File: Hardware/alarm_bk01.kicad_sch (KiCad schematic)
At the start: 18 parts, among them Q1 2N3904, SW1 START, SW2 Sensor, SW3 SW_SPDT, U1 ATtiny85V-10P

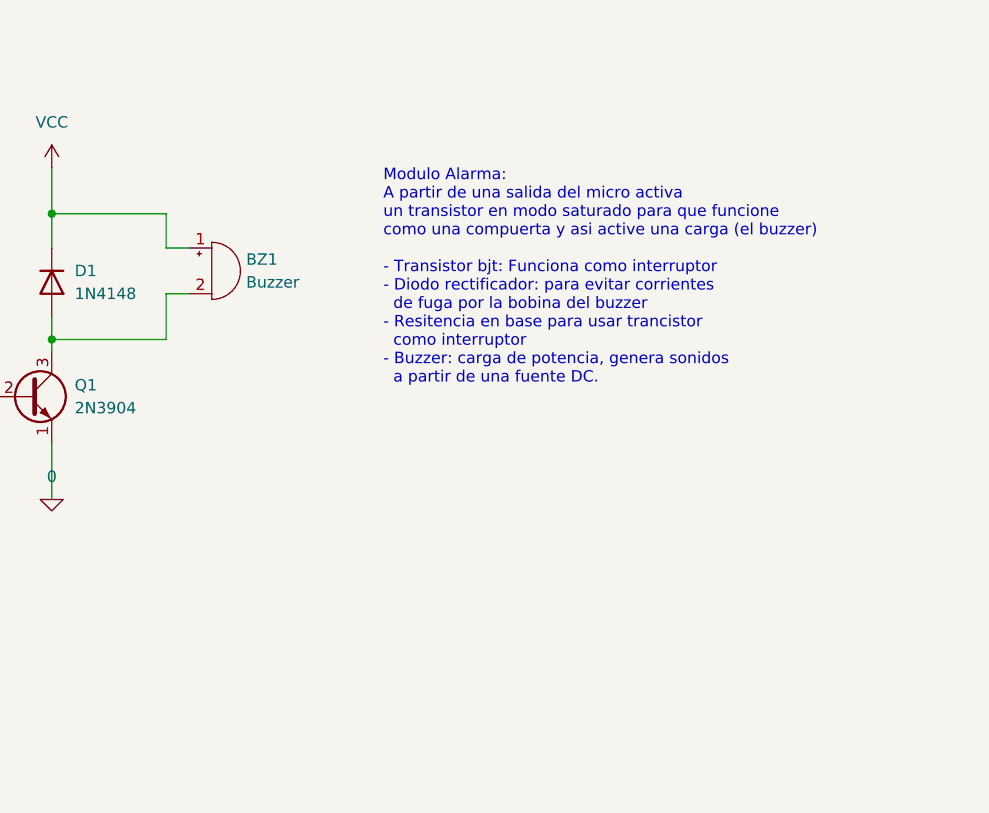
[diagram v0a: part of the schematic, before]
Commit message: reorganice components
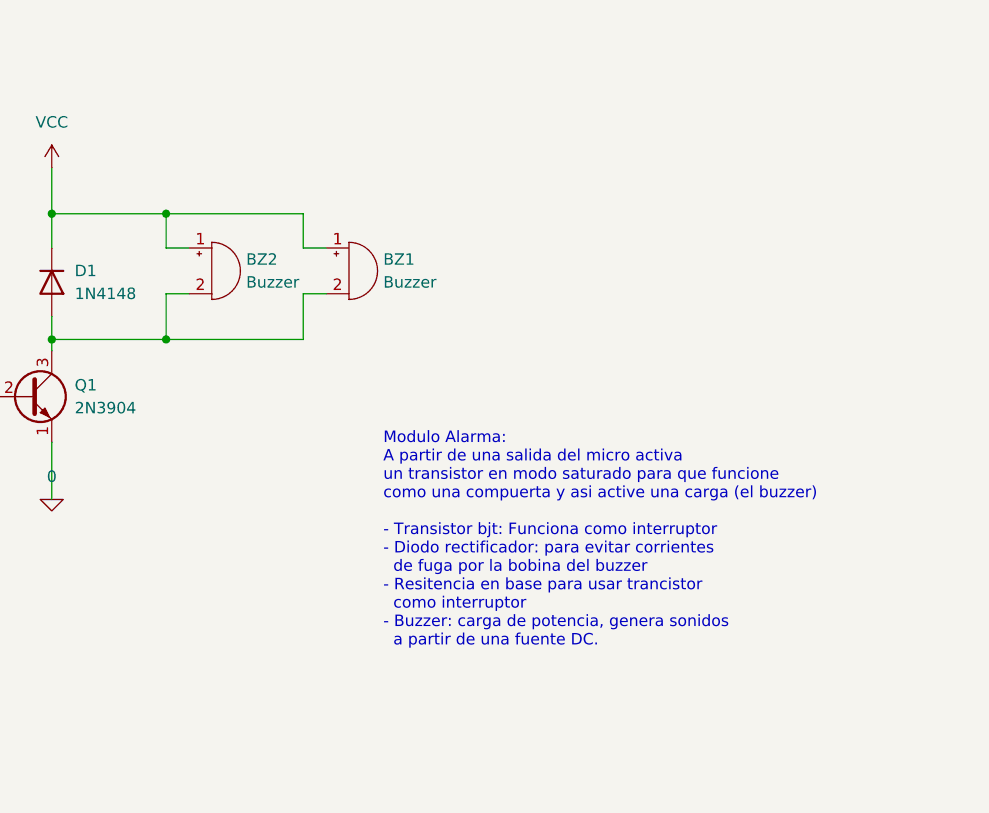
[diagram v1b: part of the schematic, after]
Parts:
- added BZ2: Buzzer, Connector_JST:JST_EH_B2B-EH-A_1x02_P2.50mm_Vertical, symbol Device:Buzzer
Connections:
- net VCC: now also BZ2.1 (-)
- net at BZ1.2 (+), D1.2 (A), Q1.3 (C): now also BZ2.2 (+)
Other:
- moved on the sheet: BZ1
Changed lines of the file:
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@@
   (junction (at 73.66 33.02) (diameter 0) (color 0 0 0 0)
   )
+  (junction (at 196.85 93.98) (diameter 0) (color 0 0 0 0)
+  )
+  (junction (at 196.85 107.95) (diameter 0) (color 0 0 0 0)
+  )
   (wire (pts (xy 69.85 181.61) (xy 69.85 186.69))
     (stroke (width 0) (type default) (color 0 0 0 0))
@@
     (stroke (width 0) (type default) (color 0 0 0 0))
   )
+  (wire (pts (xy 196.85 102.87) (xy 196.85 107.95))
+    (stroke (width 0) (type default) (color 0 0 0 0))
+  )
   (wire (pts (xy 40.64 119.38) (xy 40.64 125.73))
     (stroke (width 0) (type default) (color 0 0 0 0))
@@
     (stroke (width 0) (type default) (color 0 0 0 0))
   )
+  (wire (pts (xy 199.39 97.79) (xy 196.85 97.79))
+    (stroke (width 0) (type default) (color 0 0 0 0))
+  )
   (wire (pts (xy 140.97 24.13) (xy 140.97 30.48))
     (stroke (width 0) (type default) (color 0 0 0 0))
   )
-  (wire (pts (xy 196.85 102.87) (xy 196.85 107.95))
-    (stroke (width 0) (type default) (color 0 0 0 0))
-  )
   (wire (pts (xy 73.66 29.21) (xy 73.66 33.02))
     (stroke (width 0) (type default) (color 0 0 0 0))
@@
     (stroke (width 0) (type default) (color 0 0 0 0))
   )
-  (wire (pts (xy 196.85 102.87) (xy 199.39 102.87))
-    (stroke (width 0) (type default) (color 0 0 0 0))
-  )
   (wire (pts (xy 30.48 48.26) (xy 30.48 53.34))
     (stroke (width 0) (type default) (color 0 0 0 0))
   )
+  (wire (pts (xy 184.15 93.98) (xy 196.85 93.98))
+    (stroke (width 0) (type default) (color 0 0 0 0))
+  )
+  (wire (pts (xy 140.97 49.53) (xy 140.97 55.88))
+    (stroke (width 0) (type default) (color 0 0 0 0))
+  )
+  (wire (pts (xy 212.09 102.87) (xy 214.63 102.87))
+    (stroke (width 0) (type default) (color 0 0 0 0))
+  )
+  (wire (pts (xy 184.15 88.9) (xy 184.15 93.98))
+    (stroke (width 0) (type default) (color 0 0 0 0))
+  )
+  (wire (pts (xy 45.72 33.02) (xy 46.99 33.02))
+    (stroke (width 0) (type default) (color 0 0 0 0))
+  )
+  (wire (pts (xy 171.45 114.3) (xy 176.53 114.3))
+    (stroke (width 0) (type default) (color 0 0 0 0))
+  )
+  (wire (pts (xy 140.97 38.1) (xy 140.97 41.91))
+    (stroke (width 0) (type default) (color 0 0 0 0))
+  )
+  (wire (pts (xy 184.15 107.95) (xy 184.15 109.22))
+    (stroke (width 0) (type default) (color 0 0 0 0))
+  )
+  (wire (pts (xy 196.85 107.95) (xy 212.09 107.95))
+    (stroke (width 0) (type default) (color 0 0 0 0))
+  )
+  (wire (pts (xy 161.29 114.3) (xy 163.83 114.3))
+    (stroke (width 0) (type default) (color 0 0 0 0))
+  )
+  (wire (pts (xy 44.45 109.22) (xy 40.64 109.22))
+    (stroke (width 0) (type default) (color 0 0 0 0))
+  )
+  (wire (pts (xy 73.66 33.02) (xy 73.66 38.1))
+    (stroke (width 0) (type default) (color 0 0 0 0))
+  )
+  (wire (pts (xy 46.99 80.01) (xy 46.99 93.98))
+    (stroke (width 0) (type default) (color 0 0 0 0))
+  )
+  (wire (pts (xy 40.64 93.98) (xy 46.99 93.98))
+    (stroke (width 0) (type default) (color 0 0 0 0))
+  )
+  (wire (pts (xy 73.66 45.72) (xy 73.66 53.34))
+    (stroke (width 0) (type default) (color 0 0 0 0))
+  )
+  (wire (pts (xy 30.48 33.02) (xy 45.72 33.02))
+    (stroke (width 0) (type default) (color 0 0 0 0))
+  )
   (wire (pts (xy 196.85 97.79) (xy 196.85 93.98))
     (stroke (width 0) (type default) (color 0 0 0 0))
   )
-  (wire (pts (xy 184.15 93.98) (xy 196.85 93.98))
-    (stroke (width 0) (type default) (color 0 0 0 0))
-  )
-  (wire (pts (xy 140.97 49.53) (xy 140.97 55.88))
-    (stroke (width 0) (type default) (color 0 0 0 0))
-  )
-  (wire (pts (xy 184.15 88.9) (xy 184.15 93.98))
-    (stroke (width 0) (type default) (color 0 0 0 0))
-  )
-  (wire (pts (xy 45.72 33.02) (xy 46.99 33.02))
-    (stroke (width 0) (type default) (color 0 0 0 0))
-  )
-  (wire (pts (xy 171.45 114.3) (xy 176.53 114.3))
-    (stroke (width 0) (type default) (color 0 0 0 0))
-  )
-  (wire (pts (xy 140.97 38.1) (xy 140.97 41.91))
-    (stroke (width 0) (type default) (color 0 0 0 0))
-  )
-  (wire (pts (xy 184.15 107.95) (xy 184.15 109.22))
-    (stroke (width 0) (type default) (color 0 0 0 0))
-  )
-  (wire (pts (xy 161.29 114.3) (xy 163.83 114.3))
-    (stroke (width 0) (type default) (color 0 0 0 0))
-  )
-  (wire (pts (xy 44.45 109.22) (xy 40.64 109.22))
-    (stroke (width 0) (type default) (color 0 0 0 0))
-  )
-  (wire (pts (xy 73.66 33.02) (xy 73.66 38.1))
-    (stroke (width 0) (type default) (color 0 0 0 0))
-  )
-  (wire (pts (xy 46.99 80.01) (xy 46.99 93.98))
-    (stroke (width 0) (type default) (color 0 0 0 0))
-  )
-  (wire (pts (xy 40.64 93.98) (xy 46.99 93.98))
-    (stroke (width 0) (type default) (color 0 0 0 0))
-  )
-  (wire (pts (xy 73.66 45.72) (xy 73.66 53.34))
-    (stroke (width 0) (type default) (color 0 0 0 0))
-  )
-  (wire (pts (xy 30.48 33.02) (xy 45.72 33.02))
+  (wire (pts (xy 199.39 102.87) (xy 196.85 102.87))
     (stroke (width 0) (type default) (color 0 0 0 0))
   )
@@
     (stroke (width 0) (type default) (color 0 0 0 0))
   )
+  (wire (pts (xy 212.09 93.98) (xy 212.09 97.79))
+    (stroke (width 0) (type default) (color 0 0 0 0))
+  )
   (wire (pts (xy 57.15 33.02) (xy 62.23 33.02))
     (stroke (width 0) (type default) (color 0 0 0 0))
@@
     (stroke (width 0) (type default) (color 0 0 0 0))
   )
+  (wire (pts (xy 212.09 97.79) (xy 214.63 97.79))
+    (stroke (width 0) (type default) (color 0 0 0 0))
+  )
   (wire (pts (xy 44.45 105.41) (xy 44.45 109.22))
     (stroke (width 0) (type default) (color 0 0 0 0))
@@
     (stroke (width 0) (type default) (color 0 0 0 0))
   )
-  (wire (pts (xy 199.39 97.79) (xy 196.85 97.79))
+  (wire (pts (xy 196.85 93.98) (xy 212.09 93.98))
     (stroke (width 0) (type default) (color 0 0 0 0))
   )
@@
   )
   (wire (pts (xy 45.72 45.72) (xy 45.72 53.34))
+    (stroke (width 0) (type default) (color 0 0 0 0))
+  )
+  (wire (pts (xy 212.09 107.95) (xy 212.09 102.87))
     (stroke (width 0) (type default) (color 0 0 0 0))
   )
@@
   )
   (text "Modulo Alarma:\nA partir de una salida del micro activa \nun transistor en modo saturado para que funcione\ncomo una compuerta y asi active una carga (el buzzer)\n\n- Transistor bjt: Funciona como interruptor\n- Diodo rectificador: para evitar corrientes \n  de fuga por la bobina del buzzer\n- Resitencia en base para usar trancistor \n  como interruptor\n- Buzzer: carga de potencia, genera sonidos\n  a partir de una fuente DC."
-    (at 220.98 113.03 0)
+    (at 220.98 142.24 0)
     (effects (font (size 1.27 1.27)) (justify left bottom))
   )
@@
     (pin "2")
   )
-  (symbol (lib_id "Device:Buzzer") (at 201.93 100.33 0) (unit 1)
-    (in_bom yes) (on_board yes) (fields_autoplaced)
-    (property "Reference" "BZ1" (id 0) (at 205.74 99.0599 0)
-      (effects (font (size 1.27 1.27)) (justify left))
-    )
-    (property "Value" "Buzzer" (id 1) (at 205.74 101.5999 0)
-      (effects (font (size 1.27 1.27)) (justify left))
-    )
-    (property "Footprint" "Connector_JST:JST_EH_B2B-EH-A_1x02_P2.50mm_Vertical" (id 2) (at 201.295 97.79 90)
-      (effects (font (size 1.27 1.27)) hide)
-    )
-    (property "Datasheet" "~" (id 3) (at 201.295 97.79 90)
+  (symbol (lib_id "Device:Buzzer") (at 217.17 100.33 0) (unit 1)
+    (in_bom yes) (on_board yes) (fields_autoplaced)
+    (property "Reference" "BZ1" (id 0) (at 220.98 99.0599 0)
+      (effects (font (size 1.27 1.27)) (justify left))
+    )
+    (property "Value" "Buzzer" (id 1) (at 220.98 101.5999 0)
+      (effects (font (size 1.27 1.27)) (justify left))
+    )
+    (property "Footprint" "Connector_JST:JST_EH_B2B-EH-A_1x02_P2.50mm_Vertical" (id 2) (at 216.535 97.79 90)
+      (effects (font (size 1.27 1.27)) hide)
+    )
+    (property "Datasheet" "~" (id 3) (at 216.535 97.79 90)
       (effects (font (size 1.27 1.27)) hide)
     )
@@
     (pin "2")
     (pin "3")
+  )
+  (symbol (lib_id "Device:Buzzer") (at 201.93 100.33 0) (unit 1)
+    (in_bom yes) (on_board yes) (fields_autoplaced)
+    (property "Reference" "BZ2" (id 0) (at 205.74 99.0599 0)
+      (effects (font (size 1.27 1.27)) (justify left))
+    )
+    (property "Value" "Buzzer" (id 1) (at 205.74 101.5999 0)
+      (effects (font (size 1.27 1.27)) (justify left))
+    )
+    (property "Footprint" "Connector_JST:JST_EH_B2B-EH-A_1x02_P2.50mm_Vertical" (id 2) (at 201.295 97.79 90)
+      (effects (font (size 1.27 1.27)) hide)
+    )
+    (property "Datasheet" "~" (id 3) (at 201.295 97.79 90)
+      (effects (font (size 1.27 1.27)) hide)
+    )
+    (pin "1")
+    (pin "2")
   )
   (symbol (lib_id "MCU_Microchip_ATtiny:ATtiny85V-10P") (at 69.85 166.37 0) (mirror y) (unit 1)
@@
       (reference "BZ1") (unit 1) (value "Buzzer") (footprint "Connector_JST:JST_EH_B2B-EH-A_1x02_P2.50mm_Vertical")
     )
+    (path "/ba9d4216-b458-4eff-8d50-21ed5423f5fa"
+      (reference "BZ2") (unit 1) (value "Buzzer") (footprint "Connector_JST:JST_EH_B2B-EH-A_1x02_P2.50mm_Vertical")
+    )
     (path "/f9d78065-9a5e-4d58-b424-72b0930f1c67"

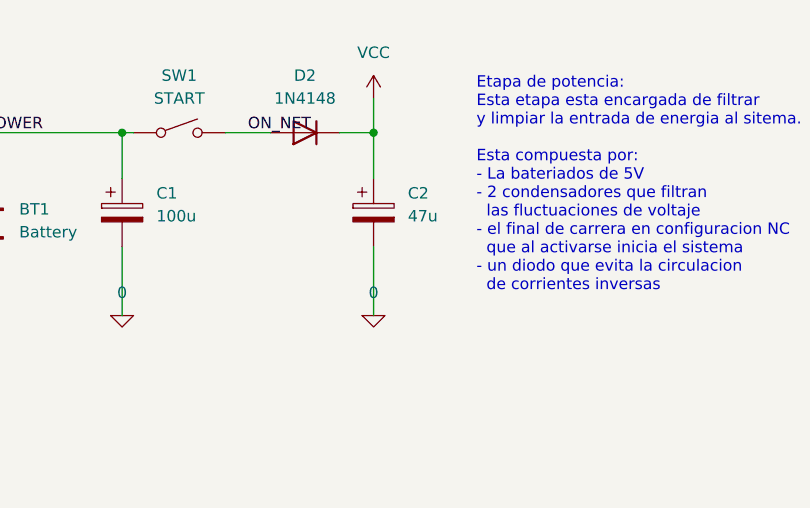
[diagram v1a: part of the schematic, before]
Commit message: add second buzzer in schematic
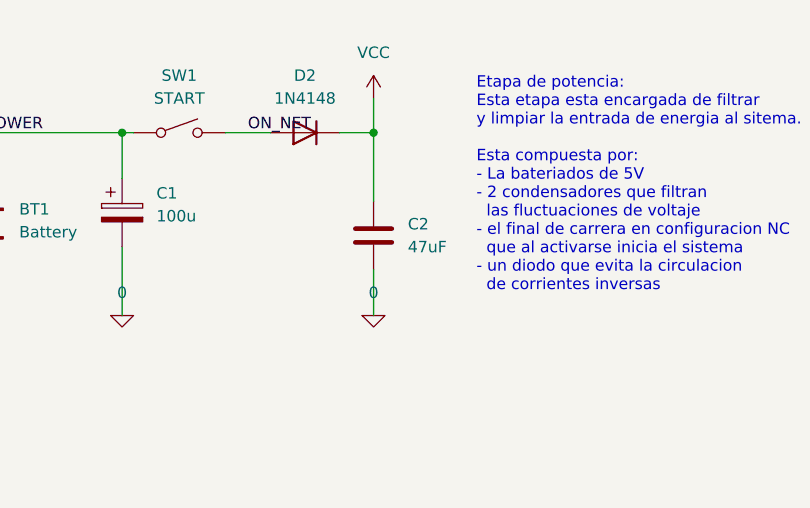
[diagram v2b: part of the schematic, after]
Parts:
- removed C2: 47u, Capacitor_THT:CP_Radial_D5.0mm_P2.00mm, symbol Device:C_Polarized
- added C2: 47uF, Capacitor_THT:C_Disc_D3.0mm_W2.0mm_P2.50mm, symbol Device:C
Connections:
- net 0: now also C2.2
- net VCC: now also C2.1
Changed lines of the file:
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@@
+    (stroke (width 0) (type default) (color 0 0 0 0))
+  )
+  (wire (pts (xy 73.66 33.02) (xy 73.66 40.64))
     (stroke (width 0) (type default) (color 0 0 0 0))
   )
@@
     (stroke (width 0) (type default) (color 0 0 0 0))
   )
-  (wire (pts (xy 73.66 33.02) (xy 73.66 38.1))
-    (stroke (width 0) (type default) (color 0 0 0 0))
-  )
   (wire (pts (xy 46.99 80.01) (xy 46.99 93.98))
     (stroke (width 0) (type default) (color 0 0 0 0))
@@
     (stroke (width 0) (type default) (color 0 0 0 0))
   )
-  (wire (pts (xy 73.66 45.72) (xy 73.66 53.34))
-    (stroke (width 0) (type default) (color 0 0 0 0))
-  )
   (wire (pts (xy 30.48 33.02) (xy 45.72 33.02))
     (stroke (width 0) (type default) (color 0 0 0 0))
@@
   )
   (wire (pts (xy 212.09 97.79) (xy 214.63 97.79))
+    (stroke (width 0) (type default) (color 0 0 0 0))
+  )
+  (wire (pts (xy 73.66 48.26) (xy 73.66 53.34))
     (stroke (width 0) (type default) (color 0 0 0 0))
   )
@@
     (pin "1")
   )
-  (symbol (lib_id "Device:C_Polarized") (at 73.66 41.91 0) (unit 1)
-    (in_bom yes) (on_board yes) (fields_autoplaced)
-    (property "Reference" "C2" (id 0) (at 77.47 39.7509 0)
-      (effects (font (size 1.27 1.27)) (justify left))
-    )
-    (property "Value" "47u" (id 1) (at 77.47 42.2909 0)
-      (effects (font (size 1.27 1.27)) (justify left))
-    )
-    (property "Footprint" "Capacitor_THT:CP_Radial_D5.0mm_P2.00mm" (id 2) (at 74.6252 45.72 0)
-      (effects (font (size 1.27 1.27)) hide)
-    )
-    (property "Datasheet" "~" (id 3) (at 73.66 41.91 0)
-      (effects (font (size 1.27 1.27)) hide)
-    )
-    (pin "1")
-    (pin "2")
-  )
   (symbol (lib_id "power:VCC") (at 69.85 147.32 0) (unit 1)
     (in_bom yes) (on_board yes) (fields_autoplaced)
@@
     )
     (property "Datasheet" "~" (id 3) (at 208.28 49.53 0)
+      (effects (font (size 1.27 1.27)) hide)
+    )
+    (pin "1")
+    (pin "2")
+  )
+  (symbol (lib_id "Device:C") (at 73.66 44.45 0) (unit 1)
+    (in_bom yes) (on_board yes) (fields_autoplaced)
+    (property "Reference" "C2" (id 0) (at 77.47 43.1799 0)
+      (effects (font (size 1.27 1.27)) (justify left))
+    )
+    (property "Value" "47uF" (id 1) (at 77.47 45.7199 0)
+      (effects (font (size 1.27 1.27)) (justify left))
+    )
+    (property "Footprint" "Capacitor_THT:C_Disc_D3.0mm_W2.0mm_P2.50mm" (id 2) (at 74.6252 48.26 0)
+      (effects (font (size 1.27 1.27)) hide)
+    )
+    (property "Datasheet" "~" (id 3) (at 73.66 44.45 0)
       (effects (font (size 1.27 1.27)) hide)
     )
@@
       (reference "C1") (unit 1) (value "100u") (footprint "Capacitor_THT:CP_Radial_D5.0mm_P2.00mm")
     )
-    (path "/36ccb50b-7274-42f5-911d-120a0977e584"
-      (reference "C2") (unit 1) (value "47u") (footprint "Capacitor_THT:CP_Radial_D5.0mm_P2.00mm")
+    (path "/8f4214c6-ba6b-411c-b7db-a13b0703b8f6"
+      (reference "C2") (unit 1) (value "47uF") (footprint "Capacitor_THT:C_Disc_D3.0mm_W2.0mm_P2.50mm")
     )
     (path "/975c72d4-2c60-4f9d-9b9c-faca6d11c853"
